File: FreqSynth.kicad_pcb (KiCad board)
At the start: 4 copper layers, 49 x 50 mm, 131 parts, among them P1 CPL-CON-BARREL-2.1MM, P2 RF1, P3 RF2, P4 CONN_01X03, P5 REF_IN, P7 SWD, U1 MAX2870, U10 PE43711, U11 LMH2110, U12 STM32F030K6T6, U2 TS5A3159, U3 TLV7113333DDSET, U4 AP65101, U5 TLV7113333DDSET, U6 RT9069-50GB, U7 SKY13322-375LF, U8 SKY13322-375LF, U9 TRF37A75, X1 25MHz ±5ppm 3.3V 33mA

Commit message: Finished routing the preliminary layout
Signed-off-by: Martin Berglund <LeastSignificantBit@users.noreply.github.com>
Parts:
- added ?: , FreqSynth:VIA, F.Cu at (134.5, 129.5)
- added ?: , FreqSynth:VIA, F.Cu at (110.0, 124.0)
- added ?: , FreqSynth:VIA, F.Cu at (133.8, 123.8)
- added ?: , FreqSynth:VIA, F.Cu at (133.0, 123.8)
- added ?: , FreqSynth:VIA, F.Cu at (133.0, 124.5)
- added ?: , FreqSynth:VIA, F.Cu at (133.8, 124.5)
- added ?: , FreqSynth:VIA, F.Cu at (135.8, 125.2)
- added ?: , FreqSynth:VIA, F.Cu at (135.8, 124.5)
- added ?: , FreqSynth:VIA, F.Cu at (136.5, 124.5)
- added ?: , FreqSynth:VIA, F.Cu at (136.5, 123.8)
- added ?: , FreqSynth:VIA, F.Cu at (135.8, 123.8)
- added ?: , FreqSynth:VIA, F.Cu at (135.8, 123.0)
- added ?: , FreqSynth:VIA, F.Cu at (120.5, 122.5)
- added ?: , FreqSynth:VIA, F.Cu at (136.5, 123.0)
- added ?: , FreqSynth:VIA, F.Cu at (138.8, 123.0)
- added ?: , FreqSynth:VIA, F.Cu at (138.8, 120.8)
- added ?: , FreqSynth:VIA, F.Cu at (138.8, 120.0)
- added ?: , FreqSynth:VIA, F.Cu at (138.8, 118.5)
- added ?: , FreqSynth:VIA, F.Cu at (138.8, 119.2)
- added ?: , FreqSynth:VIA, F.Cu at (137.2, 116.5)
- added ?: , FreqSynth:VIA, F.Cu at (138.0, 117.2)
- added ?: , FreqSynth:VIA, F.Cu at (129.8, 115.5)
- added ?: , FreqSynth:VIA, F.Cu at (129.0, 116.2)
- added ?: , FreqSynth:VIA, F.Cu at (125.0, 118.0)
- added ?: , FreqSynth:VIA, F.Cu at (128.0, 120.8)
- added ?: , FreqSynth:VIA, F.Cu at (130.2, 120.8)
- added ?: , FreqSynth:VIA, F.Cu at (130.2, 120.0)
- added ?: , FreqSynth:VIA, F.Cu at (130.2, 119.2)
- added ?: , FreqSynth:VIA, F.Cu at (131.0, 118.5)
- added ?: , FreqSynth:VIA, F.Cu at (131.0, 119.2)
- added ?: , FreqSynth:VIA, F.Cu at (131.0, 120.0)
- added ?: , FreqSynth:VIA, F.Cu at (131.0, 120.8)
- added ?: , FreqSynth:VIA, F.Cu at (136.5, 120.8)
- added ?: , FreqSynth:VIA, F.Cu at (136.5, 120.0)
- added ?: , FreqSynth:VIA, F.Cu at (113.5, 112.0)
- added ?: , FreqSynth:VIA, F.Cu at (136.5, 119.2)
- added ?: , FreqSynth:VIA, F.Cu at (135.8, 118.5)
- added ?: , FreqSynth:VIA, F.Cu at (135.8, 119.2)
- added ?: , FreqSynth:VIA, F.Cu at (135.8, 120.0)
- added ?: , FreqSynth:VIA, F.Cu at (135.8, 120.8)
- added ?: , FreqSynth:VIA, F.Cu at (133.8, 120.8)
- added ?: , FreqSynth:VIA, F.Cu at (133.8, 120.0)
- added ?: , FreqSynth:VIA, F.Cu at (133.8, 119.2)
- added ?: , FreqSynth:VIA, F.Cu at (133.0, 119.2)
- added ?: , FreqSynth:VIA, F.Cu at (133.0, 120.0)
- added ?: , FreqSynth:VIA, F.Cu at (147.5, 134.5)
- added ?: , FreqSynth:VIA, F.Cu at (133.0, 120.8)
- added ?: , FreqSynth:VIA, F.Cu at (143.0, 134.5)
- added ?: , FreqSynth:VIA, F.Cu at (143.0, 137.5)
- added ?: , FreqSynth:VIA, F.Cu at (147.5, 129.5)
- added ?: , FreqSynth:VIA, F.Cu at (147.5, 137.5)
- added ?: , FreqSynth:VIA, F.Cu at (140.0, 142.0)
- added ?: , FreqSynth:VIA, F.Cu at (108.0, 116.0)
- added ?: , FreqSynth:VIA, F.Cu at (137.0, 144.5)
- added ?: , FreqSynth:VIA, F.Cu at (122.0, 128.5)
- added ?: , FreqSynth:VIA, F.Cu at (121.5, 137.5)
- added ?: , FreqSynth:VIA, F.Cu at (117.0, 141.0)
- added ?: , FreqSynth:VIA, F.Cu at (104.5, 149.0)
- added ?: , FreqSynth:VIA, F.Cu at (113.0, 149.0)
- added ?: , FreqSynth:VIA, F.Cu at (123.5, 149.0)
- added ?: , FreqSynth:VIA, F.Cu at (133.5, 149.0)
- added ?: , FreqSynth:VIA, F.Cu at (141.0, 149.0)
- added ?: , FreqSynth:VIA, F.Cu at (147.5, 149.0)
- added ?: , FreqSynth:VIA, F.Cu at (124.0, 146.5)
- added ?: , FreqSynth:VIA, F.Cu at (106.5, 146.0)
- added ?: , FreqSynth:VIA, F.Cu at (104.0, 135.5)
- added ?: , FreqSynth:VIA, F.Cu at (105.5, 112.0)
- added ?: , FreqSynth:VIA, F.Cu at (105.5, 101.5)
- added ?: , FreqSynth:VIA, F.Cu at (113.5, 101.5)
- added ?: , FreqSynth:VIA, F.Cu at (120.0, 101.5)
- added ?: , FreqSynth:VIA, F.Cu at (128.5, 101.5)
- added ?: , FreqSynth:VIA, F.Cu at (138.0, 101.5)
- added ?: , FreqSynth:VIA, F.Cu at (148.0, 101.5)
- added ?: , FreqSynth:VIA, F.Cu at (147.5, 115.0)
- added ?: , FreqSynth:VIA, F.Cu at (123.0, 140.5)
- added ?: , FreqSynth:VIA, F.Cu at (143.0, 115.0)
- added ?: , FreqSynth:VIA, F.Cu at (143.0, 112.0)
- added ?: , FreqSynth:VIA, F.Cu at (143.0, 117.5)
- added ?: , FreqSynth:VIA, F.Cu at (147.5, 117.5)
- added ?: , FreqSynth:VIA, F.Cu at (147.5, 112.0)
- added ?: , FreqSynth:VIA, F.Cu at (124.0, 108.0)
- added ?: , FreqSynth:VIA, F.Cu at (128.0, 108.0)
- added ?: , FreqSynth:VIA, F.Cu at (124.0, 110.5)
- added ?: , FreqSynth:VIA, F.Cu at (124.0, 113.5)
- added ?: , FreqSynth:VIA, F.Cu at (128.0, 110.5)
- added ?: , FreqSynth:VIA, F.Cu at (128.0, 143.0)
- added ?: , FreqSynth:VIA, F.Cu at (124.0, 125.0)
- added ?: , FreqSynth:VIA, F.Cu at (130.8, 128.8)
- added ?: , FreqSynth:VIA, F.Cu at (139.8, 122.2)
- added ?: , FreqSynth:VIA, F.Cu at (141.5, 121.8)
- added ?: , FreqSynth:VIA, F.Cu at (142.0, 125.0)
- added ?: , FreqSynth:VIA, F.Cu at (141.2, 125.2)
- added ?: , FreqSynth:VIA, F.Cu at (141.4, 126.4)
- added ?: , FreqSynth:VIA, F.Cu at (138.8, 126.2)
- added ?: , FreqSynth:VIA, F.Cu at (138.2, 127.2)
- added ?: , FreqSynth:VIA, F.Cu at (136.8, 128.8)
- added ?: , FreqSynth:VIA, F.Cu at (112.0, 133.5)
- added ?: , FreqSynth:VIA, F.Cu at (139.0, 129.5)
- added ?: , FreqSynth:VIA, F.Cu at (136.0, 129.5)
- added ?: , FreqSynth:VIA, F.Cu at (135.2, 130.2)
- added ?: , FreqSynth:VIA, F.Cu at (134.5, 131.0)
- added ?: , FreqSynth:VIA, F.Cu at (138.0, 109.5)
- added ?: , FreqSynth:VIA, F.Cu at (138.8, 108.5)
- added ?: , FreqSynth:VIA, F.Cu at (138.8, 109.5)
- added ?: , FreqSynth:VIA, F.Cu at (141.0, 109.5)
- added ?: , FreqSynth:VIA, F.Cu at (141.0, 108.5)
- added ?: , FreqSynth:VIA, F.Cu at (141.2, 107.8)
- added ?: , FreqSynth:VIA, F.Cu at (114.0, 133.5)
- added ?: , FreqSynth:VIA, F.Cu at (141.2, 102.2)
- added ?: , FreqSynth:VIA, F.Cu at (141.2, 103.5)
- added ?: , FreqSynth:VIA, F.Cu at (141.2, 104.8)
- added ?: , FreqSynth:VIA, F.Cu at (142.0, 105.2)
- added ?: , FreqSynth:VIA, F.Cu at (141.2, 105.8)
- added ?: , FreqSynth:VIA, F.Cu at (140.5, 105.8)
- added ?: , FreqSynth:VIA, F.Cu at (139.8, 105.8)
- added ?: , FreqSynth:VIA, F.Cu at (135.0, 108.0)
- added ?: , FreqSynth:VIA, F.Cu at (133.8, 106.0)
- added ?: , FreqSynth:VIA, F.Cu at (133.2, 106.5)
- added ?: , FreqSynth:VIA, F.Cu at (106.0, 124.0)
- added ?: , FreqSynth:VIA, F.Cu at (134.5, 108.5)
- added ?: , FreqSynth:VIA, F.Cu at (135.5, 108.8)
- added ?: , FreqSynth:VIA, F.Cu at (135.5, 110.8)
- added ?: , FreqSynth:VIA, F.Cu at (135.5, 112.0)
- added ?: , FreqSynth:VIA, F.Cu at (134.8, 113.2)
- added ?: , FreqSynth:VIA, F.Cu at (135.5, 115.0)
- added ?: , FreqSynth:VIA, F.Cu at (129.0, 126.8)
- added ?: , FreqSynth:VIA, F.Cu at (128.0, 126.0)
- added ?: , FreqSynth:VIA, F.Cu at (128.0, 125.2)
- added ?: , FreqSynth:VIA, F.Cu at (128.0, 124.5)
- added ?: , FreqSynth:VIA, F.Cu at (106.0, 120.5)
- added ?: , FreqSynth:VIA, F.Cu at (128.0, 123.8)
- added ?: , FreqSynth:VIA, F.Cu at (131.0, 125.2)
- added ?: , FreqSynth:VIA, F.Cu at (130.2, 124.5)
- added ?: , FreqSynth:VIA, F.Cu at (131.0, 124.5)
- added ?: , FreqSynth:VIA, F.Cu at (131.0, 123.8)
- added ?: , FreqSynth:VIA, F.Cu at (130.2, 123.8)
- added ?: , FreqSynth:VIA, F.Cu at (130.2, 123.0)
- added ?: , FreqSynth:VIA, F.Cu at (131.0, 123.0)
- added ?: , FreqSynth:VIA, F.Cu at (133.0, 123.0)
- added ?: , FreqSynth:VIA, F.Cu at (133.8, 123.0)
- added G***: LOGO, FreqSynth:Logo_silk_polarity_center_5x1.4mm, B.Cu at (102.8, 106.8)
- added G***: LOGO, FreqSynth:Logo_silk_WEEE_3.4x5mm, B.Cu at (115.0, 145.5)
- added G***: LOGO, FreqSynth:Logo_silk_OSHW_6x6mm, B.Cu at (128.8, 144.8)
- moved C22 6.09 mm to (127.5, 146.2), turned to 180 degrees
- moved R15 5.77 mm to (103.5, 117.0), turned to 90 degrees
- moved C23 3.82 mm to (130.8, 144.5)
- moved L22 3.64 mm to (118.0, 147.2), turned to 180 degrees
- moved C17 3.35 mm to (133.2, 134.2), turned to 0 degrees
- moved R19 2.55 mm to (103.5, 121.5), turned to 90 degrees
- moved C66 1.80 mm to (115.5, 147.2), turned to 180 degrees
- moved D2 1.59 mm to (102.0, 117.0), turned to 90 degrees
- moved D3 1.50 mm to (102.0, 121.5)
- moved X1 1.12 mm to (130.5, 147.0), turned to 0 degrees
- moved C11 1.00 mm to (128.8, 129.5)
- moved C20 0.83 mm to (137.0, 133.2)
- moved C64 0.71 mm to (110.2, 148.0)
- moved C65 0.71 mm to (110.2, 146.5)
- moved C19 0.61 mm to (137.0, 134.8)
- gave numbers to parts that had none: 2
- renumbered P7 to P6, R15 to R16, R16 to R17, R17 to R18
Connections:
- U12 pad 10: /MCU/EXT_CLK_EN -> /MCU/LD_PLL
- U12 pad 11: /MCU/LD_PLL -> /MCU/CS_PLL
- U12 pad 12: /Amplifier/ATTEN_CS -> /MCU/CE_PLL
- U12 pad 13: /FILT1 -> /MCU/ADC1
- U12 pad 14: Net-(D3-Pad1) -> /FILT2
- U12 pad 15: Net-(U12-Pad15) -> /FILT3
- U12 pad 18: /FILT2 -> /FILT4
- U12 pad 19: /FILT3 -> /FILT1
- U12 pad 20: /FILT4 -> /Amplifier/PWDN
- U12 pad 21: /MCU/EN_PLL -> /Amplifier/ATTEN_CS
- U12 pad 22: /MCU/CE_PLL -> Net-(D3-Pad1)
- U12 pad 25: /MCU/CS_PLL -> Net-(U12-Pad25)
- U12 pad 8: Net-(U12-Pad8) -> /MCU/EXT_CLK_EN
- U12 pad 9: /MCU/ADC1 -> /MCU/EN_PLL
- U9 pad 5: Earth -> /Amplifier/PWDN
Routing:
- net /MOSI: track 1.16 -> 77.3 mm, vias 1 -> 3
- net /SCK: track 1.26 -> 76.2 mm, vias 1 -> 4
- net /MCU/VCC_D: track 27.4 -> 77.6 mm, vias 2 -> 9
- net /MCU/ADC1: track 0.62 -> 43.6 mm, vias 1 -> 2
- net /Amplifier/ATTEN_CS: track 0.00 -> 39.1 mm, vias 0 -> 2
- net /Amplifier/PWDN: track 0.00 -> 38.7 mm, vias 0 -> 2
- net /Power/VCC_D: track 7.78 -> 44.1 mm, vias 0 -> 2
- net /MISO: track 0.77 -> 31.1 mm, vias 1 -> 2
- net /3v3: track 28.0 -> 57.2 mm, vias 4 -> 7
- net Earth: track 88.9 -> 115.8 mm, vias 19 -> 47
- net /MCU/CE_PLL: track 0.70 -> 24.8 mm, vias 1 -> 2
- net Net-(D3-Pad1): track 0.00 -> 24.0 mm
- net /FILT4: track 9.50 -> 33.1 mm, vias 2 -> 3
- net /PLL/VCC_RF: track 12.9 -> 36.2 mm, vias 1 -> 3
- net /FILT3: track 9.37 -> 31.5 mm, vias 2 -> 3
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- added copper zone on B.Cu, net Earth
- added copper zone on In2.Cu, net Earth
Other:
- board text added: "SWD"
- board text added: "https://github.com/LeastSignificantBit/FreqSynth"

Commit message: Added new leds and switched swd header to 0.1" instead of jst
Signed-off-by: Martin Berglund <LeastSignificantBit@users.noreply.github.com>
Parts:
- D2, D3: footprint LEDs:LED_0603 -> LEDs:LED-3MM
- P6: footprint Connectors_JST:JST_SHL_SM05B-SHLS-TF_05x1.00mm_Angled -> Pin_Headers:Pin_Header_Straight_2x03
- R15, R19: value 33R -> 180R
- moved ? 4.92 mm to (101.9, 117.8)
- moved R15 3.90 mm to (107.0, 115.2)
- moved R19 3.68 mm to (107.0, 120.3)
- moved ? 2.80 mm to (108.3, 143.8)
- moved P6 1.90 mm to (103.2, 140.6), turned to 0 degrees
- moved D2 1.88 mm to (103.8, 116.5)
- moved D3 1.81 mm to (103.8, 121.6)
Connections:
- D3 pad 1: Net-(D3-Pad1) -> Earth
- R19 pad 1: /MCU/VCC_D -> Net-(R19-Pad1)
- U12 pad 22: Net-(D3-Pad1) -> Net-(R19-Pad1)
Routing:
- net Net-(D3-Pad1): track 24.0 -> 0.00 mm
- net Net-(R19-Pad1): track 0.00 -> 23.1 mm
- net /MCU/VCC_D: track 77.6 -> 57.0 mm, vias 9 -> 6
- net Net-(P6-Pad5): track 10.6 -> 13.7 mm
- net Net-(D3-Pad2): track 1.50 -> 3.39 mm
- net Net-(D2-Pad2): track 1.50 -> 3.39 mm
- net Earth: track 115.8 -> 114.7 mm, vias 47 -> 46
- net /Power/VCC_D: track 44.1 -> 43.1 mm

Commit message: fixed the barreljack
Signed-off-by: Martin Berglund <LeastSignificantBit@users.noreply.github.com>
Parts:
- P1: footprint Connect:BARREL_JACK -> FreqSynth:BARREL_JACK
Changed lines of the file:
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@@
   (general
     (links 461)
-    (no_connects 3)
+    (no_connects 0)
     (area 100.424999 99.924999 149.575001 150.075001)
     (thickness 1.6)
@@
   )
   (setup
-    (last_trace_width 0.254)
+    (last_trace_width 0.127)
     (user_trace_width 0.1905)
     (user_trace_width 0.254)
@@
     )
   )
-  (module Connect:BARREL_JACK (layer F.Cu)
-    (at 105.79986 106.5)
-    (descr "DC Barrel Jack")
-    (tags "Power Jack")
-    (fp_text reference P1 (at 10.09904 0 90) (layer F.SilkS) hide
-      (effects (font (size 0.4 0.4) (thickness 0.1)))
-    )
-    (fp_text value CPL-CON-BARREL-2.1MM (at 0 -5.99948) (layer F.Fab)
-      (effects (font (size 1 1) (thickness 0.15)))
-    )
-    (fp_line (start -4.0005 -4.50088) (end -4.0005 4.50088) (layer F.SilkS) (width 0.15))
-    (fp_line (start -7.50062 -4.50088) (end -7.50062 4.50088) (layer F.SilkS) (width 0.15))
-    (fp_line (start -7.50062 4.50088) (end 7.00024 4.50088) (layer F.SilkS) (width 0.15))
-    (fp_line (start 7.00024 4.50088) (end 7.00024 -4.50088) (layer F.SilkS) (width 0.15))
-    (fp_line (start 7.00024 -4.50088) (end -7.50062 -4.50088) (layer F.SilkS) (width 0.15))
-    (pad 1 thru_hole rect (at 6.20014 0) (size 3.50012 3.50012) (drill oval 1.00076 2.99974) (layers *.Cu *.Mask F.SilkS)
-      (net 62 "Net-(P1-Pad1)"))
-    (pad 2 thru_hole rect (at 0.20066 0) (size 3.50012 3.50012) (drill oval 1.00076 2.99974) (layers *.Cu *.Mask F.SilkS)
-      (net 8 Earth))
-    (pad 3 thru_hole rect (at 3.2004 4.699) (size 3.50012 3.50012) (drill oval 2.99974 1.00076) (layers *.Cu *.Mask F.SilkS)
-      (net 8 Earth))
-  )
   (module FreqSynth:SMA_edge (layer F.Cu)
     (at 145 106.75)
@@
     )
   )
+  (module FreqSynth:BARREL_JACK (layer F.Cu)
+    (at 105.79986 106.5)
+    (descr "EJ508A 2.1 barrel jack")
+    (tags "Power Jack")
+    (fp_text reference P1 (at 10.09904 0 90) (layer F.SilkS) hide
+      (effects (font (size 0.4 0.4) (thickness 0.1)))
+    )
+    (fp_text value CPL-CON-BARREL-2.1MM (at 0 -5.99948) (layer F.Fab)
+      (effects (font (size 1 1) (thickness 0.15)))
+    )
+    (fp_line (start -4.0005 -4.50088) (end -4.0005 4.50088) (layer F.SilkS) (width 0.15))
+    (fp_line (start -7.50062 -4.50088) (end -7.50062 4.50088) (layer F.SilkS) (width 0.15))
+    (fp_line (start -7.50062 4.50088) (end 7.00024 4.50088) (layer F.SilkS) (width 0.15))
+    (fp_line (start 7.00024 4.50088) (end 7.00024 -4.50088) (layer F.SilkS) (width 0.15))
+    (fp_line (start 7.00024 -4.50088) (end -7.50062 -4.50088) (layer F.SilkS) (width 0.15))
+    (pad 1 thru_hole rect (at 6.5 0) (size 3.50012 3.80012) (drill oval 1.02 3.5) (layers *.Cu *.Mask F.SilkS)
+      (net 62 "Net-(P1-Pad1)"))
+    (pad 2 thru_hole rect (at 0 0) (size 3.5 3.8) (drill oval 1.02 3.5) (layers *.Cu *.Mask F.SilkS)
+      (net 8 Earth))
+    (pad 3 thru_hole rect (at 3.25 4.5) (size 3.7 3.5) (drill oval 3.05 1) (layers *.Cu *.Mask F.SilkS)
+      (net 8 Earth))
+  )
   (gr_text https://github.com/LeastSignificantBit/FreqSynth (at 123.25 123.75) (layer B.SilkS)

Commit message: All ICS duble-checked! some RF solved
Signed-off-by: Martin Berglund <LeastSignificantBit@users.noreply.github.com>
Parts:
- added ?: , FreqSynth:VIA, F.Cu at (134.9, 114.6)
- added ?: , FreqSynth:VIA, F.Cu at (131.1, 115.2)
- C57, C58: moved to B.Cu
- moved C58 1.20 mm to (131.1, 112.7)
- moved C57 0.73 mm to (131.1, 114.0)
- moved ? 0.57 mm to (135.5, 111.4)
- moved ? 0.19 mm to (134.9, 113.3)
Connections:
- net /MCU/EXT_CLK_EN renamed /MCU/INT_CLK_EN
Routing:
- net Earth: track 114.7 -> 140.4 mm, vias 46 -> 48
- net /Amplifier/PWDN: track 38.7 -> 40.7 mm
- net /Amplifier/3V3: track 17.2 -> 15.5 mm

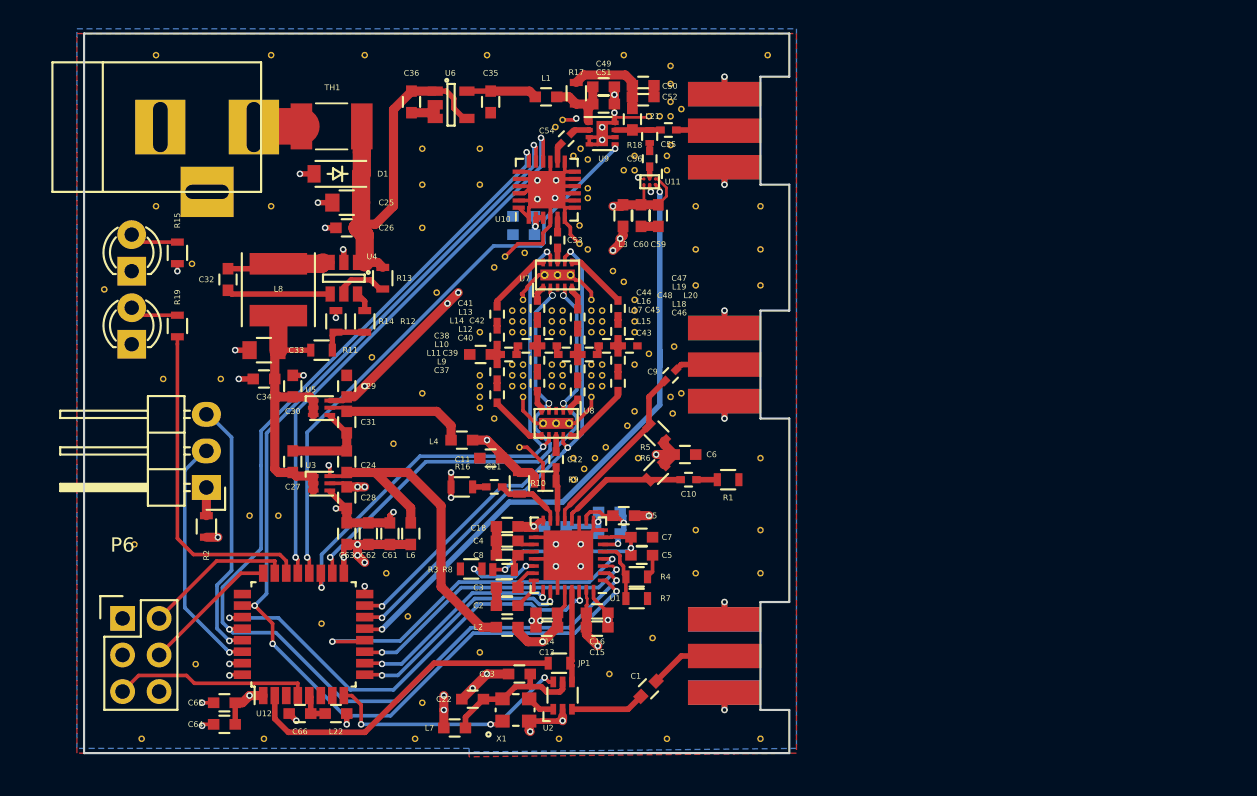
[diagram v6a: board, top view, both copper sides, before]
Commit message: reroutet the entire board
Signed-off-by: Martin Berglund <LeastSignificantBit@users.noreply.github.com>
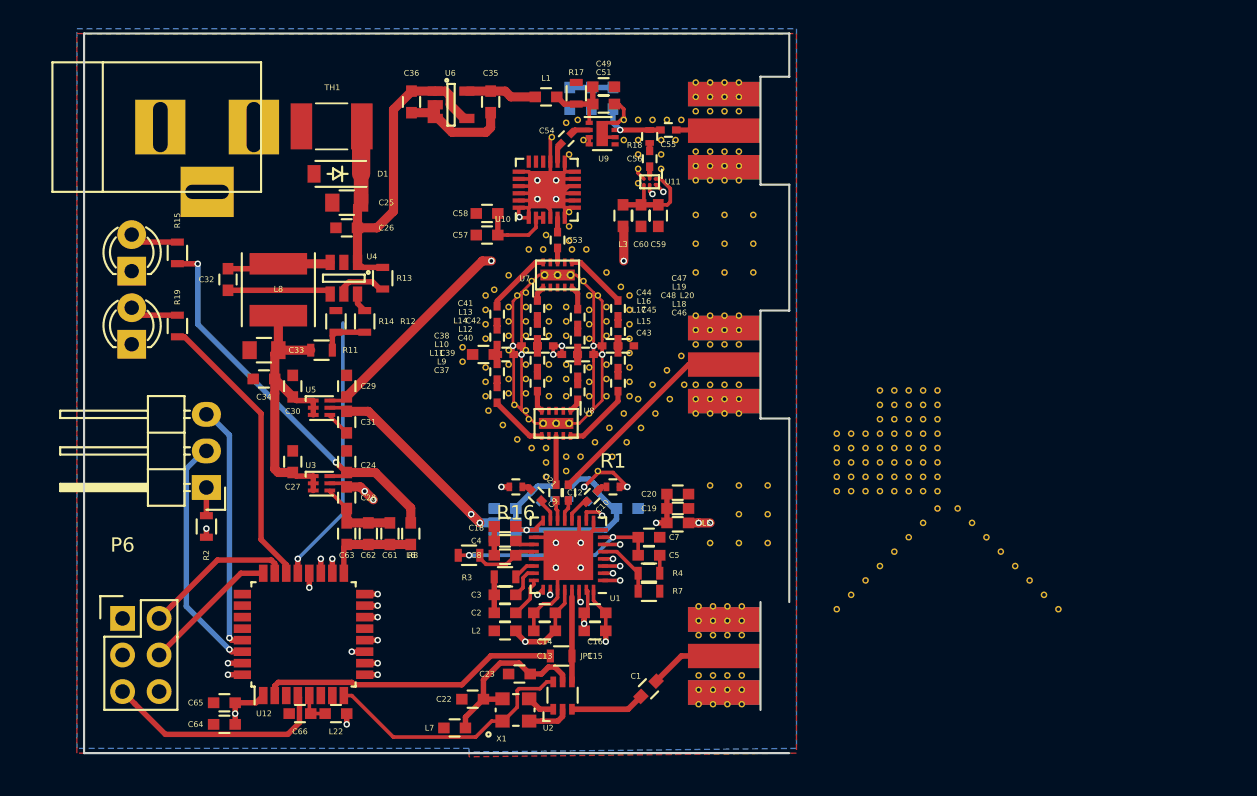
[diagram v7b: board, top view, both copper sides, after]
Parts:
- removed the ? at (134.9, 114.6)
- removed the ? at (106.0, 124.0)
- removed the ? at (133.0, 123.0)
- removed the ? at (133.8, 123.0)
- removed the ? at (133.8, 123.8)
- removed the ? at (133.0, 123.8)
- removed the ? at (133.0, 124.5)
- removed the ? at (133.8, 124.5)
- removed the ? at (135.8, 125.2)
- removed the ? at (135.8, 124.5)
- removed the ? at (136.5, 124.5)
- removed the ? at (136.5, 123.8)
- removed the ? at (101.9, 117.8)
- removed the ? at (135.8, 123.8)
- removed the ? at (135.8, 123.0)
- removed the ? at (136.5, 123.0)
- removed the ? at (138.8, 123.0)
- removed the ? at (138.8, 120.8)
- removed the ? at (138.8, 120.0)
- removed the ? at (138.8, 118.5)
- removed the ? at (138.8, 119.2)
- removed the ? at (137.2, 116.5)
- removed the ? at (138.0, 117.2)
- removed the ? at (110.0, 124.0)
- removed the ? at (129.8, 115.5)
- removed the ? at (129.0, 116.2)
- removed the ? at (128.0, 120.8)
- removed the ? at (130.2, 120.8)
- removed the ? at (130.2, 120.0)
- removed the ? at (130.2, 119.2)
- removed the ? at (131.0, 118.5)
- removed the ? at (131.0, 119.2)
- removed the ? at (131.0, 120.0)
- removed the ? at (131.0, 120.8)
- removed the ? at (120.5, 122.5)
- removed the ? at (136.5, 120.8)
- removed the ? at (136.5, 120.0)
- removed the ? at (136.5, 119.2)
- removed the ? at (135.8, 118.5)
- removed the ? at (135.8, 119.2)
- removed the ? at (135.8, 120.0)
- removed the ? at (135.8, 120.8)
- removed the ? at (133.8, 120.8)
- removed the ? at (133.8, 120.0)
- removed the ? at (133.8, 119.2)
- removed the ? at (125.0, 118.0)
- removed the ? at (133.0, 119.2)
- removed the ? at (133.0, 120.0)
- removed the ? at (133.0, 120.8)
- removed the ? at (113.5, 112.0)
- removed the ? at (147.5, 134.5)
- removed the ? at (143.0, 134.5)
- removed the ? at (143.0, 137.5)
- removed the ? at (147.5, 129.5)
- removed the ? at (131.1, 115.2)
- removed the ? at (147.5, 137.5)
- removed the ? at (140.0, 142.0)
- removed the ? at (137.0, 144.5)
- removed the ? at (122.0, 128.5)
- removed the ? at (121.5, 137.5)
- removed the ? at (117.0, 141.0)
- removed the ? at (104.5, 149.0)
- removed the ? at (113.0, 149.0)
- removed the ? at (123.5, 149.0)
- removed the ? at (133.5, 149.0)
- removed the ? at (134.5, 129.5)
- removed the ? at (141.0, 149.0)
- removed the ? at (147.5, 149.0)
- removed the ? at (108.3, 143.8)
- removed the ? at (104.0, 135.5)
- removed the ? at (105.5, 112.0)
- removed the ? at (105.5, 101.5)
- removed the ? at (113.5, 101.5)
- removed the ? at (120.0, 101.5)
- removed the ? at (128.5, 101.5)
- removed the ? at (138.0, 101.5)
- removed the ? at (108.0, 116.0)
- removed the ? at (148.0, 101.5)
- removed the ? at (147.5, 115.0)
- removed the ? at (143.0, 115.0)
- removed the ? at (143.0, 112.0)
- removed the ? at (143.0, 117.5)
- removed the ? at (147.5, 117.5)
- removed the ? at (147.5, 112.0)
- removed the ? at (124.0, 108.0)
- removed the ? at (128.0, 108.0)
- removed the ? at (124.0, 110.5)
- removed the ? at (124.0, 146.5)
- removed the ? at (124.0, 113.5)
- removed the ? at (128.0, 110.5)
- removed the ? at (124.0, 125.0)
- removed the ? at (130.8, 128.8)
- removed the ? at (139.8, 122.2)
- removed the ? at (141.5, 121.8)
- removed the ? at (142.0, 125.0)
- removed the ? at (141.2, 125.2)
- removed the ? at (141.4, 126.4)
- removed the ? at (138.8, 126.2)
- removed the ? at (123.0, 140.5)
- removed the ? at (138.2, 127.2)
- removed the ? at (136.8, 128.8)
- removed the ? at (139.0, 129.5)
- removed the ? at (136.0, 129.5)
- removed the ? at (135.2, 130.2)
- removed the ? at (134.5, 131.0)
- removed the ? at (138.0, 109.5)
- removed the ? at (138.8, 108.5)
- removed the ? at (138.8, 109.5)
- removed the ? at (141.0, 109.5)
- removed the ? at (128.0, 143.0)
- removed the ? at (141.0, 108.5)
- removed the ? at (141.2, 107.8)
- removed the ? at (141.2, 102.2)
- removed the ? at (141.2, 103.5)
- removed the ? at (141.2, 104.8)
- removed the ? at (142.0, 105.2)
- removed the ? at (141.2, 105.8)
- removed the ? at (140.5, 105.8)
- removed the ? at (139.8, 105.8)
- removed the ? at (135.0, 108.0)
- removed the ? at (112.0, 133.5)
- removed the ? at (133.8, 106.0)
- removed the ? at (133.2, 106.5)
- removed the ? at (134.5, 108.5)
- removed the ? at (135.5, 108.8)
- removed the ? at (135.5, 110.8)
- removed the ? at (135.5, 111.4)
- removed the ? at (134.9, 113.3)
- removed the ? at (135.5, 115.0)
- removed the ? at (129.0, 126.8)
- removed the ? at (128.0, 126.0)
- removed the ? at (114.0, 133.5)
- removed the ? at (128.0, 125.2)
- removed the ? at (128.0, 124.5)
- removed the ? at (128.0, 123.8)
- removed the ? at (131.0, 125.2)
- removed the ? at (130.2, 124.5)
- removed the ? at (131.0, 124.5)
- removed the ? at (131.0, 123.8)
- removed the ? at (130.2, 123.8)
- removed the ? at (130.2, 123.0)
- removed the ? at (131.0, 123.0)
- removed G***: LOGO, FreqSynth:Logo_silk_polarity_center_5x1.4mm
- removed G***: LOGO, FreqSynth:Logo_silk_WEEE_3.4x5mm
- removed G***: LOGO, FreqSynth:Logo_silk_OSHW_6x6mm
- added ?: , FreqSynth:VIA, F.Cu at (148.0, 135.4)
- added ?: , FreqSynth:VIA, F.Cu at (147.0, 116.6)
- added ?: , FreqSynth:VIA, F.Cu at (131.6, 117.2)
- added ?: , FreqSynth:VIA, F.Cu at (130.0, 125.0)
- added ?: , FreqSynth:VIA, F.Cu at (130.0, 121.0)
- added ?: , FreqSynth:VIA, F.Cu at (130.0, 120.0)
- added ?: , FreqSynth:VIA, F.Cu at (130.0, 119.0)
- added ?: , FreqSynth:VIA, F.Cu at (130.0, 124.0)
- added ?: , FreqSynth:VIA, F.Cu at (130.0, 123.0)
- added ?: , FreqSynth:VIA, F.Cu at (130.0, 122.0)
- added ?: , FreqSynth:VIA, F.Cu at (131.2, 126.2)
- added ?: , FreqSynth:VIA, F.Cu at (131.2, 125.0)
- added ?: , FreqSynth:VIA, F.Cu at (143.0, 116.6)
- added ?: , FreqSynth:VIA, F.Cu at (131.2, 124.0)
- added ?: , FreqSynth:VIA, F.Cu at (131.2, 120.0)
- added ?: , FreqSynth:VIA, F.Cu at (131.2, 119.0)
- added ?: , FreqSynth:VIA, F.Cu at (131.2, 118.0)
- added ?: , FreqSynth:VIA, F.Cu at (131.2, 123.0)
- added ?: , FreqSynth:VIA, F.Cu at (131.2, 122.0)
- added ?: , FreqSynth:VIA, F.Cu at (131.2, 121.0)
- added ?: , FreqSynth:VIA, F.Cu at (132.8, 125.2)
- added ?: , FreqSynth:VIA, F.Cu at (132.8, 123.0)
- added ?: , FreqSynth:VIA, F.Cu at (132.8, 124.0)
- added ?: , FreqSynth:VIA, F.Cu at (143.0, 114.6)
- added ?: , FreqSynth:VIA, F.Cu at (132.8, 119.0)
- added ?: , FreqSynth:VIA, F.Cu at (132.8, 120.0)
- added ?: , FreqSynth:VIA, F.Cu at (132.8, 121.0)
- added ?: , FreqSynth:VIA, F.Cu at (134.0, 125.2)
- added ?: , FreqSynth:VIA, F.Cu at (134.0, 123.0)
- added ?: , FreqSynth:VIA, F.Cu at (134.0, 124.0)
- added ?: , FreqSynth:VIA, F.Cu at (134.0, 119.0)
- added ?: , FreqSynth:VIA, F.Cu at (134.0, 120.0)
- added ?: , FreqSynth:VIA, F.Cu at (134.0, 121.0)
- added ?: , FreqSynth:VIA, F.Cu at (146.0, 125.4)
- added ?: , FreqSynth:VIA, F.Cu at (145.0, 116.6)
- added ?: , FreqSynth:VIA, F.Cu at (145.0, 124.4)
- added ?: , FreqSynth:VIA, F.Cu at (145.0, 125.4)
- added ?: , FreqSynth:VIA, F.Cu at (146.0, 124.4)
- added ?: , FreqSynth:VIA, F.Cu at (144.0, 125.4)
- added ?: , FreqSynth:VIA, F.Cu at (144.0, 124.4)
- added ?: , FreqSynth:VIA, F.Cu at (143.0, 125.4)
- added ?: , FreqSynth:VIA, F.Cu at (143.0, 124.4)
- added ?: , FreqSynth:VIA, F.Cu at (146.0, 121.6)
- added ?: , FreqSynth:VIA, F.Cu at (145.0, 120.6)
- added ?: , FreqSynth:VIA, F.Cu at (145.0, 121.6)
- added ?: , FreqSynth:VIA, F.Cu at (145.0, 114.6)
- added ?: , FreqSynth:VIA, F.Cu at (146.0, 120.6)
- added ?: , FreqSynth:VIA, F.Cu at (144.0, 121.6)
- added ?: , FreqSynth:VIA, F.Cu at (144.0, 120.6)
- added ?: , FreqSynth:VIA, F.Cu at (143.0, 121.6)
- added ?: , FreqSynth:VIA, F.Cu at (143.0, 120.6)
- added ?: , FreqSynth:VIA, F.Cu at (142.0, 122.4)
- added ?: , FreqSynth:VIA, F.Cu at (135.4, 115.0)
- added ?: , FreqSynth:VIA, F.Cu at (134.4, 115.0)
- added ?: , FreqSynth:VIA, F.Cu at (132.4, 115.0)
- added ?: , FreqSynth:VIA, F.Cu at (131.4, 115.0)
- added ?: , FreqSynth:VIA, F.Cu at (147.0, 114.6)
- added ?: , FreqSynth:VIA, F.Cu at (129.0, 117.8)
- added ?: , FreqSynth:VIA, F.Cu at (130.0, 116.8)
- added ?: , FreqSynth:VIA, F.Cu at (136.2, 118.2)
- added ?: , FreqSynth:VIA, F.Cu at (135.2, 117.2)
- added ?: , FreqSynth:VIA, F.Cu at (136.8, 125.2)
- added ?: , FreqSynth:VIA, F.Cu at (136.8, 124.0)
- added ?: , FreqSynth:VIA, F.Cu at (136.8, 123.0)
- added ?: , FreqSynth:VIA, F.Cu at (136.8, 119.0)
- added ?: , FreqSynth:VIA, F.Cu at (136.8, 120.0)
- added ?: , FreqSynth:VIA, F.Cu at (136.8, 121.0)
- added ?: , FreqSynth:VIA, F.Cu at (145.0, 112.6)
- added ?: , FreqSynth:VIA, F.Cu at (135.6, 126.4)
- added ?: , FreqSynth:VIA, F.Cu at (135.6, 125.2)
- added ?: , FreqSynth:VIA, F.Cu at (135.6, 124.2)
- added ?: , FreqSynth:VIA, F.Cu at (135.6, 119.2)
- added ?: , FreqSynth:VIA, F.Cu at (135.6, 118.2)
- added ?: , FreqSynth:VIA, F.Cu at (135.6, 120.2)
- added ?: , FreqSynth:VIA, F.Cu at (135.6, 123.2)
- added ?: , FreqSynth:VIA, F.Cu at (135.6, 121.2)
- added ?: , FreqSynth:VIA, F.Cu at (138.4, 123.2)
- added ?: , FreqSynth:VIA, F.Cu at (138.4, 124.2)
- added ?: , FreqSynth:VIA, F.Cu at (147.0, 112.6)
- added ?: , FreqSynth:VIA, F.Cu at (138.4, 125.2)
- added ?: , FreqSynth:VIA, F.Cu at (138.4, 118.2)
- added ?: , FreqSynth:VIA, F.Cu at (138.4, 119.2)
- added ?: , FreqSynth:VIA, F.Cu at (138.4, 120.2)
- added ?: , FreqSynth:VIA, F.Cu at (138.4, 122.2)
- added ?: , FreqSynth:VIA, F.Cu at (138.4, 121.2)
- added ?: , FreqSynth:VIA, F.Cu at (137.8, 117.6)
- added ?: , FreqSynth:VIA, F.Cu at (136.8, 116.6)
- added ?: , FreqSynth:VIA, F.Cu at (128.4, 125.2)
- added ?: , FreqSynth:VIA, F.Cu at (128.4, 124.2)
- added ?: , FreqSynth:VIA, F.Cu at (145.0, 126.4)
- added ?: , FreqSynth:VIA, F.Cu at (128.4, 123.2)
- added ?: , FreqSynth:VIA, F.Cu at (128.4, 118.2)
- added ?: , FreqSynth:VIA, F.Cu at (128.4, 119.2)
- added ?: , FreqSynth:VIA, F.Cu at (128.4, 120.2)
- added ?: , FreqSynth:VIA, F.Cu at (129.6, 127.2)
- added ?: , FreqSynth:VIA, F.Cu at (130.6, 128.2)
- added ?: , FreqSynth:VIA, F.Cu at (128.6, 126.2)
- added ?: , FreqSynth:VIA, F.Cu at (131.6, 128.8)
- added ?: , FreqSynth:VIA, F.Cu at (134.0, 129.4)
- added ?: , FreqSynth:VIA, F.Cu at (141.2, 125.4)
- added ?: , FreqSynth:VIA, F.Cu at (146.0, 126.4)
- added ?: , FreqSynth:VIA, F.Cu at (142.2, 124.4)
- added ?: , FreqSynth:VIA, F.Cu at (138.2, 128.4)
- added ?: , FreqSynth:VIA, F.Cu at (139.2, 127.4)
- added ?: , FreqSynth:VIA, F.Cu at (137.2, 129.4)
- added ?: , FreqSynth:VIA, F.Cu at (140.2, 126.4)
- added ?: , FreqSynth:VIA, F.Cu at (136.2, 130.4)
- added ?: , FreqSynth:VIA, F.Cu at (132.6, 130.8)
- added ?: , FreqSynth:VIA, F.Cu at (132.6, 129.8)
- added ?: , FreqSynth:VIA, F.Cu at (132.6, 128.8)
- added ?: , FreqSynth:VIA, F.Cu at (139.0, 125.4)
- added ?: , FreqSynth:VIA, F.Cu at (148.0, 131.4)
- added ?: , FreqSynth:VIA, F.Cu at (144.0, 126.4)
- added ?: , FreqSynth:VIA, F.Cu at (140.0, 124.4)
- added ?: , FreqSynth:VIA, F.Cu at (141.0, 123.4)
- added ?: , FreqSynth:VIA, F.Cu at (138.0, 126.4)
- added ?: , FreqSynth:VIA, F.Cu at (134.0, 130.4)
- added ?: , FreqSynth:VIA, F.Cu at (135.0, 129.4)
- added ?: , FreqSynth:VIA, F.Cu at (137.0, 127.4)
- added ?: , FreqSynth:VIA, F.Cu at (136.0, 128.4)
- added ?: , FreqSynth:VIA, F.Cu at (165.2, 137.0)
- added ?: , FreqSynth:VIA, F.Cu at (161.2, 133.0)
- added ?: , FreqSynth:VIA, F.Cu at (167.2, 139.0)
- added ?: , FreqSynth:VIA, F.Cu at (143.0, 126.4)
- added ?: , FreqSynth:VIA, F.Cu at (164.2, 136.0)
- added ?: , FreqSynth:VIA, F.Cu at (166.2, 138.0)
- added ?: , FreqSynth:VIA, F.Cu at (162.2, 134.0)
- added ?: , FreqSynth:VIA, F.Cu at (163.2, 135.0)
- added ?: , FreqSynth:VIA, F.Cu at (168.2, 140.0)
- added ?: , FreqSynth:VIA, F.Cu at (155.8, 137.0)
- added ?: , FreqSynth:VIA, F.Cu at (159.8, 133.0)
- added ?: , FreqSynth:VIA, F.Cu at (153.8, 139.0)
- added ?: , FreqSynth:VIA, F.Cu at (156.8, 136.0)
- added ?: , FreqSynth:VIA, F.Cu at (154.8, 138.0)
- added ?: , FreqSynth:VIA, F.Cu at (146.0, 119.6)
- added ?: , FreqSynth:VIA, F.Cu at (158.8, 134.0)
- added ?: , FreqSynth:VIA, F.Cu at (157.8, 135.0)
- added ?: , FreqSynth:VIA, F.Cu at (152.8, 140.0)
- added ?: , FreqSynth:VIA, F.Cu at (158.8, 128.8)
- added ?: , FreqSynth:VIA, F.Cu at (159.8, 128.8)
- added ?: , FreqSynth:VIA, F.Cu at (159.8, 129.8)
- added ?: , FreqSynth:VIA, F.Cu at (158.8, 129.8)
- added ?: , FreqSynth:VIA, F.Cu at (156.8, 130.8)
- added ?: , FreqSynth:VIA, F.Cu at (157.8, 130.8)
- added ?: , FreqSynth:VIA, F.Cu at (155.8, 130.8)
- added ?: , FreqSynth:VIA, F.Cu at (145.0, 119.6)
- added ?: , FreqSynth:VIA, F.Cu at (157.8, 128.8)
- added ?: , FreqSynth:VIA, F.Cu at (155.8, 128.8)
- added ?: , FreqSynth:VIA, F.Cu at (156.8, 128.8)
- added ?: , FreqSynth:VIA, F.Cu at (156.8, 129.8)
- added ?: , FreqSynth:VIA, F.Cu at (157.8, 129.8)
- added ?: , FreqSynth:VIA, F.Cu at (152.8, 130.8)
- added ?: , FreqSynth:VIA, F.Cu at (153.8, 130.8)
- added ?: , FreqSynth:VIA, F.Cu at (153.8, 128.8)
- added ?: , FreqSynth:VIA, F.Cu at (152.8, 129.8)
- added ?: , FreqSynth:VIA, F.Cu at (154.8, 128.8)
- added ?: , FreqSynth:VIA, F.Cu at (143.0, 119.6)
- added ?: , FreqSynth:VIA, F.Cu at (154.8, 130.8)
- added ?: , FreqSynth:VIA, F.Cu at (152.8, 128.8)
- added ?: , FreqSynth:VIA, F.Cu at (153.8, 129.8)
- added ?: , FreqSynth:VIA, F.Cu at (157.8, 131.8)
- added ?: , FreqSynth:VIA, F.Cu at (158.8, 131.8)
- added ?: , FreqSynth:VIA, F.Cu at (158.8, 130.8)
- added ?: , FreqSynth:VIA, F.Cu at (159.8, 130.8)
- added ?: , FreqSynth:VIA, F.Cu at (159.8, 131.8)
- added ?: , FreqSynth:VIA, F.Cu at (156.8, 131.8)
- added ?: , FreqSynth:VIA, F.Cu at (152.8, 131.8)
- added ?: , FreqSynth:VIA, F.Cu at (144.0, 119.6)
- added ?: , FreqSynth:VIA, F.Cu at (154.8, 129.8)
- added ?: , FreqSynth:VIA, F.Cu at (154.8, 131.8)
- added ?: , FreqSynth:VIA, F.Cu at (155.8, 131.8)
- added ?: , FreqSynth:VIA, F.Cu at (155.8, 129.8)
- added ?: , FreqSynth:VIA, F.Cu at (153.8, 131.8)
- added ?: , FreqSynth:VIA, F.Cu at (157.8, 127.8)
- added ?: , FreqSynth:VIA, F.Cu at (156.8, 126.8)
- added ?: , FreqSynth:VIA, F.Cu at (159.8, 127.8)
- added ?: , FreqSynth:VIA, F.Cu at (158.8, 126.8)
- added ?: , FreqSynth:VIA, F.Cu at (159.8, 126.8)
- added ?: , FreqSynth:VIA, F.Cu at (146.2, 146.6)
- added ?: , FreqSynth:VIA, F.Cu at (156.8, 127.8)
- added ?: , FreqSynth:VIA, F.Cu at (157.8, 126.8)
- added ?: , FreqSynth:VIA, F.Cu at (158.8, 127.8)
- added ?: , FreqSynth:VIA, F.Cu at (154.8, 127.8)
- added ?: , FreqSynth:VIA, F.Cu at (155.8, 126.8)
- added ?: , FreqSynth:VIA, F.Cu at (153.8, 127.8)
- added ?: , FreqSynth:VIA, F.Cu at (155.8, 127.8)
- added ?: , FreqSynth:VIA, F.Cu at (126.8, 122.8)
- added ?: , FreqSynth:VIA, F.Cu at (152.8, 127.8)
- added ?: , FreqSynth:VIA, F.Cu at (158.8, 124.8)
- added ?: , FreqSynth:VIA, F.Cu at (146.2, 145.6)
- added ?: , FreqSynth:VIA, F.Cu at (159.8, 125.8)
- added ?: , FreqSynth:VIA, F.Cu at (159.8, 124.8)
- added ?: , FreqSynth:VIA, F.Cu at (156.8, 124.8)
- added ?: , FreqSynth:VIA, F.Cu at (156.8, 125.8)
- added ?: , FreqSynth:VIA, F.Cu at (158.8, 125.8)
- added ?: , FreqSynth:VIA, F.Cu at (157.8, 124.8)
- added ?: , FreqSynth:VIA, F.Cu at (157.8, 125.8)
- added ?: , FreqSynth:VIA, F.Cu at (155.8, 125.8)
- added ?: , FreqSynth:VIA, F.Cu at (128.4, 121.2)
- added ?: , FreqSynth:VIA, F.Cu at (155.8, 124.8)
- added ?: , FreqSynth:VIA, F.Cu at (143.2, 144.6)
- added ?: , FreqSynth:VIA, F.Cu at (126.8, 121.8)
- added ?: , FreqSynth:VIA, F.Cu at (146.2, 144.6)
- added ?: , FreqSynth:VIA, F.Cu at (148.0, 133.4)
- added ?: , FreqSynth:VIA, F.Cu at (144.2, 146.6)
- added ?: , FreqSynth:VIA, F.Cu at (143.2, 146.6)
- added ?: , FreqSynth:VIA, F.Cu at (145.2, 146.6)
- added ?: , FreqSynth:VIA, F.Cu at (144.2, 145.6)
- added ?: , FreqSynth:VIA, F.Cu at (145.2, 145.6)
- added ?: , FreqSynth:VIA, F.Cu at (144.2, 144.6)
- added ?: , FreqSynth:VIA, F.Cu at (145.2, 144.6)
- added ?: , FreqSynth:VIA, F.Cu at (143.2, 145.6)
- added ?: , FreqSynth:VIA, F.Cu at (145.2, 139.8)
- added ?: , FreqSynth:VIA, F.Cu at (145.2, 140.8)
- added ?: , FreqSynth:VIA, F.Cu at (146.0, 131.4)
- added ?: , FreqSynth:VIA, F.Cu at (146.2, 140.8)
- added ?: , FreqSynth:VIA, F.Cu at (146.2, 139.8)
- added ?: , FreqSynth:VIA, F.Cu at (145.2, 141.8)
- added ?: , FreqSynth:VIA, F.Cu at (146.2, 141.8)
- added ?: , FreqSynth:VIA, F.Cu at (143.2, 141.8)
- added ?: , FreqSynth:VIA, F.Cu at (143.2, 140.8)
- added ?: , FreqSynth:VIA, F.Cu at (144.2, 141.8)
- added ?: , FreqSynth:VIA, F.Cu at (144.2, 140.8)
- added ?: , FreqSynth:VIA, F.Cu at (144.2, 139.8)
- added ?: , FreqSynth:VIA, F.Cu at (143.2, 139.8)
- added ?: , FreqSynth:VIA, F.Cu at (146.0, 133.4)
- added ?: , FreqSynth:VIA, F.Cu at (144.0, 108.2)
- added ?: , FreqSynth:VIA, F.Cu at (144.0, 109.2)
- added ?: , FreqSynth:VIA, F.Cu at (145.0, 108.2)
- added ?: , FreqSynth:VIA, F.Cu at (145.0, 109.2)
- added ?: , FreqSynth:VIA, F.Cu at (143.0, 109.2)
- added ?: , FreqSynth:VIA, F.Cu at (143.0, 108.2)
- added ?: , FreqSynth:VIA, F.Cu at (146.0, 108.2)
- added ?: , FreqSynth:VIA, F.Cu at (145.0, 110.2)
- added ?: , FreqSynth:VIA, F.Cu at (146.0, 109.2)
- added ?: , FreqSynth:VIA, F.Cu at (146.0, 110.2)
- added ?: , FreqSynth:VIA, F.Cu at (146.0, 135.4)
- added ?: , FreqSynth:VIA, F.Cu at (144.0, 110.2)
- added ?: , FreqSynth:VIA, F.Cu at (143.0, 110.2)
- added ?: , FreqSynth:VIA, F.Cu at (144.0, 104.4)
- added ?: , FreqSynth:VIA, F.Cu at (145.0, 104.4)
- added ?: , FreqSynth:VIA, F.Cu at (145.0, 105.4)
- added ?: , FreqSynth:VIA, F.Cu at (146.0, 104.4)
- added ?: , FreqSynth:VIA, F.Cu at (144.0, 105.4)
- added ?: , FreqSynth:VIA, F.Cu at (146.0, 105.4)
- added ?: , FreqSynth:VIA, F.Cu at (145.0, 103.4)
- added ?: , FreqSynth:VIA, F.Cu at (146.0, 103.4)
- added ?: , FreqSynth:VIA, F.Cu at (144.0, 131.4)
- added ?: , FreqSynth:VIA, F.Cu at (143.0, 105.4)
- added ?: , FreqSynth:VIA, F.Cu at (144.0, 103.4)
- added ?: , FreqSynth:VIA, F.Cu at (143.0, 103.4)
- added ?: , FreqSynth:VIA, F.Cu at (143.0, 104.4)
- added ?: , FreqSynth:VIA, F.Cu at (140.6, 109.4)
- added ?: , FreqSynth:VIA, F.Cu at (140.6, 108.4)
- added ?: , FreqSynth:VIA, F.Cu at (140.6, 107.4)
- added ?: , FreqSynth:VIA, F.Cu at (139.0, 108.4)
- added ?: , FreqSynth:VIA, F.Cu at (139.0, 109.4)
- added ?: , FreqSynth:VIA, F.Cu at (139.0, 110.4)
- added ?: , FreqSynth:VIA, F.Cu at (144.0, 135.4)
- added ?: , FreqSynth:VIA, F.Cu at (134.0, 106.2)
- added ?: , FreqSynth:VIA, F.Cu at (133.0, 107.2)
- added ?: , FreqSynth:VIA, F.Cu at (134.8, 106.0)
- added ?: , FreqSynth:VIA, F.Cu at (134.2, 108.4)
- added ?: , FreqSynth:VIA, F.Cu at (135.2, 107.4)
- added ?: , FreqSynth:VIA, F.Cu at (141.6, 107.4)
- added ?: , FreqSynth:VIA, F.Cu at (139.0, 107.4)
- added ?: , FreqSynth:VIA, F.Cu at (138.0, 107.4)
- added ?: , FreqSynth:VIA, F.Cu at (138.0, 106.0)
- added ?: , FreqSynth:VIA, F.Cu at (139.0, 106.0)
- added ?: , FreqSynth:VIA, F.Cu at (143.0, 112.6)
- added ?: , FreqSynth:VIA, F.Cu at (142.0, 106.0)
- added ?: , FreqSynth:VIA, F.Cu at (140.0, 106.0)
- added ?: , FreqSynth:VIA, F.Cu at (141.0, 106.0)
- added ?: , FreqSynth:VIA, F.Cu at (132.6, 114.0)
- added ?: , FreqSynth:VIA, F.Cu at (134.2, 113.4)
- added ?: , FreqSynth:VIA, F.Cu at (134.2, 114.4)
- added ?: , FreqSynth:VIA, F.Cu at (134.2, 112.4)
- added ?: , FreqSynth:VIA, F.Cu at (130.4, 125.8)
- added ?: , FreqSynth:VIA, F.Cu at (131.4, 126.8)
- added ?: , FreqSynth:VIA, F.Cu at (130.6, 118.2)
- C11, C50, C52, C6, L21, L4: moved to B.Cu
- C19, C20, C57, C58: moved to F.Cu
- R1, R16: footprint Resistors_SMD:R_0603 -> Resistors_SMD:R_0402
- R10, R5, R6, R9: footprint Resistors_SMD:R_0603 -> Resistors_SMD:R_0402; moved to B.Cu
- moved C9 10.8 mm to (134.2, 131.9), turned to 270 degrees
- moved R1 8.02 mm to (137.2, 131.5)
- moved R5 7.34 mm to (134.2, 131.9), turned to 270 degrees
- moved C10 6.80 mm to (135.8, 132.2), turned to 225 degrees
- moved L4 6.49 mm to (129.8, 134.0)
- moved C6 5.48 mm to (138.2, 133.0)
- moved C50 5.18 mm to (134.2, 104.5), turned to 270 degrees
- moved C19 5.06 mm to (141.8, 133.0), turned to 0 degrees
- moved C20 4.91 mm to (141.8, 132.0), turned to 0 degrees
- moved R6 4.75 mm to (135.8, 132.2)
- moved L5 3.78 mm to (141.8, 134.0)
- moved R16 3.75 mm to (130.5, 131.5)
- moved C11 3.64 mm to (129.8, 133.0)
- moved C52 3.60 mm to (135.8, 104.5), turned to 90 degrees
- moved C17 3.58 mm to (129.8, 135.0), turned to 180 degrees
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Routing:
- net /MOSI: track 77.3 -> 0.70 mm, vias 3 -> 1
- net /SCK: track 76.2 -> 1.20 mm, vias 4 -> 1
- net /MCU/VCC_D: track 57.0 -> 10.9 mm, vias 6 -> 2
- net /MCU/ADC1: track 43.6 -> 0.76 mm, vias 2 -> 1
- net /Amplifier/PWDN: track 40.7 -> 1.00 mm, vias 2 -> 1
- net /FILT1: track 38.0 -> 1.00 mm, vias 3 -> 1
- net /FILT2: track 35.3 -> 0.90 mm, vias 3 -> 1
- net /FILT4: track 33.1 -> 1.00 mm, vias 3 -> 1
- net /FILT3: track 31.5 -> 0.90 mm, vias 3 -> 1
- net /3v3: track 57.2 -> 26.9 mm, vias 7 -> 2
- net /MISO: track 31.1 -> 0.89 mm, vias 2 -> 1
- net /MCU/CE_PLL: track 24.8 -> 1.60 mm
- net /Amplifier/ATTEN_CS: track 39.1 -> 18.7 mm, vias 2 -> 1
- net /MCU/CS_PLL: track 21.0 -> 2.10 mm
- net /PLL/VCC_RF: track 36.1 -> 20.3 mm, vias 3 -> 1
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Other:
- outline, holes or cut-outs redrawn
